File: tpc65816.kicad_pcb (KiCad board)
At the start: 2 copper layers, 100 x 100 mm, 51 parts, among them J1 Barrel_Jack, J2 PORTA, J3 PORTB, J4 SD_CARD, J5 PORTD, J6 PORTC, Q1 Q_PNP_BCE, Q2 Q_NPN_BCE, SW1 RESET, U1 74HC00, U10 WD65C22, U11 WD65C22, U2 74LS245, U3 L7805, U4 WD65C816S, U5 74LS573, U6 IS61C5128AS-25QLI, U7 28C256, U8 74F521, U9 74HC00

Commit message: Edit to main schematic and layout
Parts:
- SD CARD: renamed from J4
- moved BUSY 9.94 mm to (173.3, 109.2)
- moved R6 5.66 mm to (171.2, 99.6)
- moved C4 3.28 mm to (159.5, 82.0), turned to 270 degrees
- moved C5 3.02 mm to (139.4, 95.5), turned to 90 degrees
- moved R5 1.34 mm to (164.4, 102.1)
- moved Q2 0.44 mm to (163.3, 95.2)
- moved Q1 0.20 mm to (176.0, 100.7)
- renumbered D4 to BUSY, D3 to EMU, J2 to PORTA, J3 to PORTB, J6 to PORTC, J5 to PORTD, D2 to POWER, SW1 to RESET
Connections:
- U10 pad 39: GND -> (no net)
- U10 pad 40: GND -> (no net)
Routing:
- net +5V: track 669.7 -> 681.5 mm, vias 3 -> 2
- net Net-(D4-Pad1): track 2.36 -> 13.8 mm
- net Net-(D4-Pad2): track 3.66 -> 11.0 mm
- net Net-(Q2-Pad2): track 2.90 -> 7.28 mm
- net GND: vias 21 -> 17
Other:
- board text added: "PRELIMIARY"

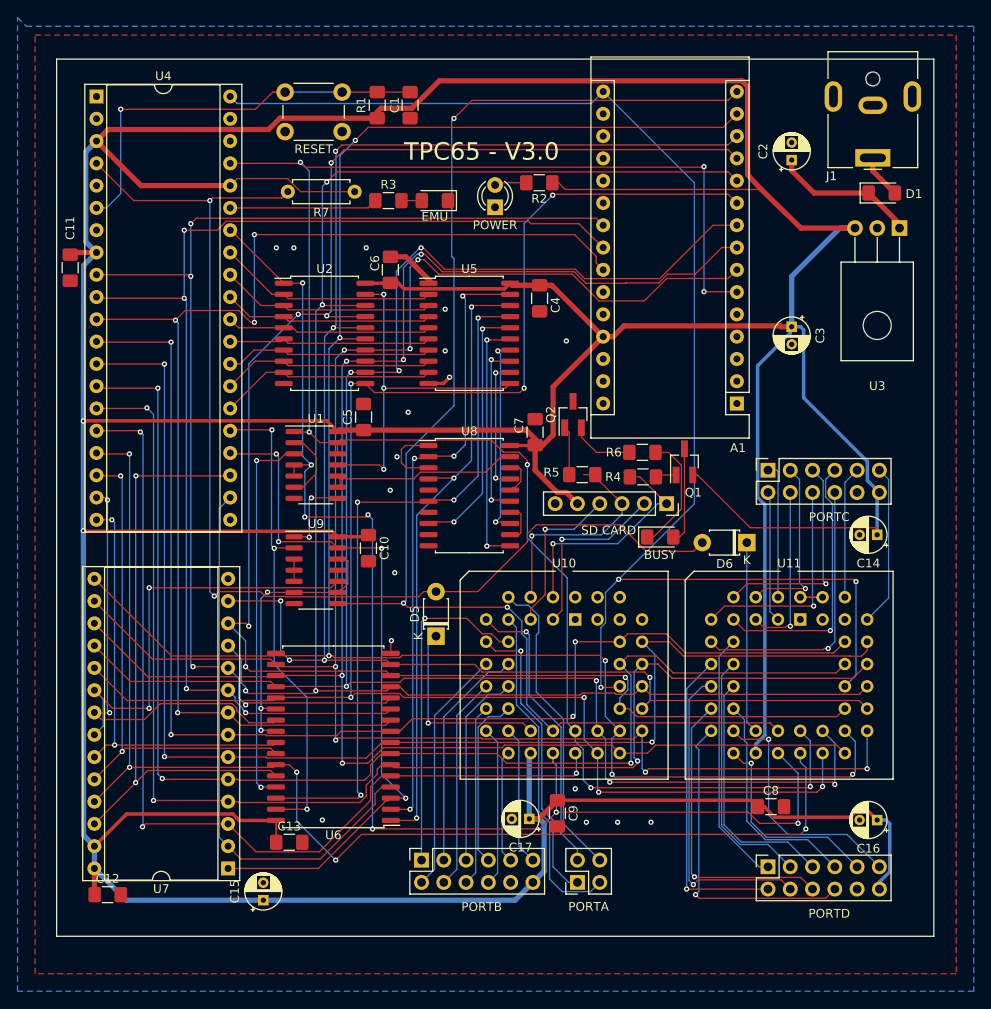
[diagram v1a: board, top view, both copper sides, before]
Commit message: Minor cleanup and repositioning - fabricated
Schematic verified. Added power switch. Repositioned PORT A. Cleanup of some traces. Added silkscreen markings. 

Board has been sent to fabrication as of this commit.
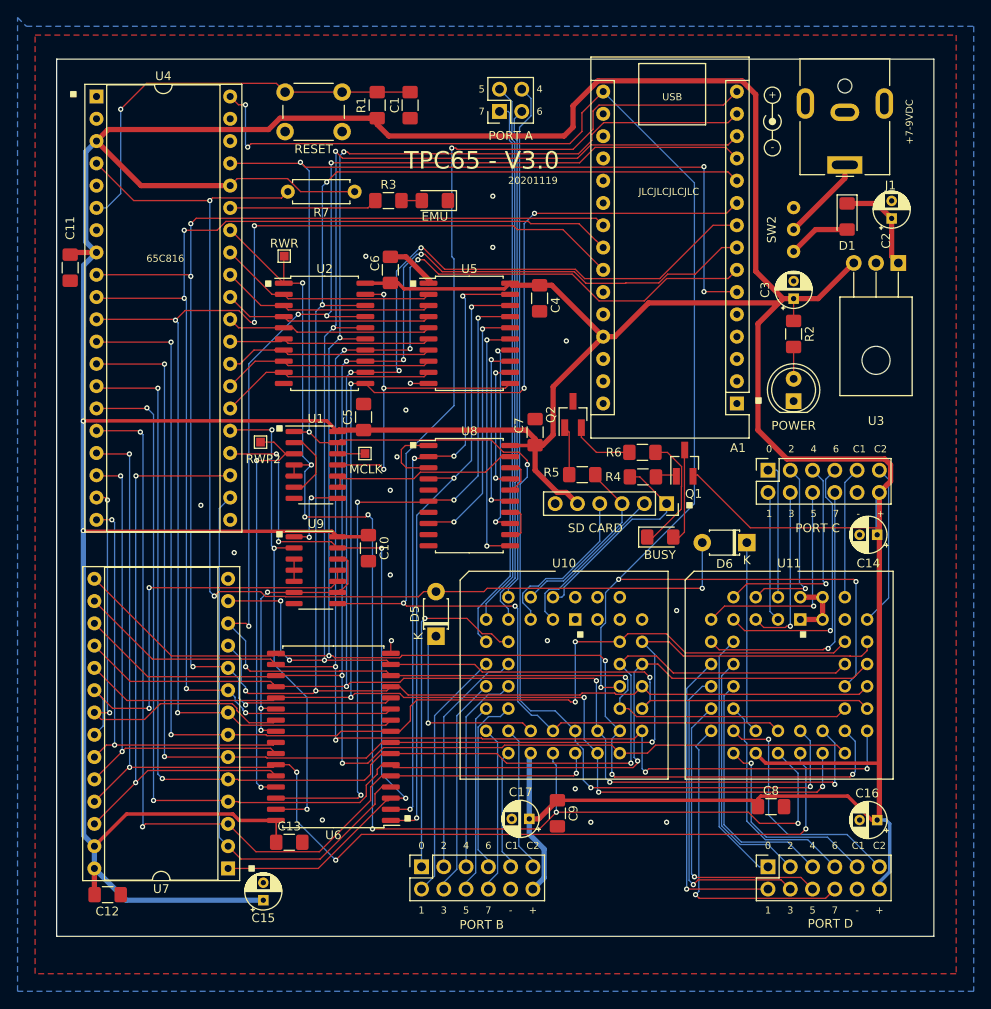
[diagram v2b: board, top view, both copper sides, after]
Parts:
- removed PORTA: PORTA, Connector_PinSocket_2.54mm:PinSocket_2x02_P2.54mm_Vertical
- removed the POWER at (154.4, 71.6)
- added MCLK: MCLK, TestPoint:TestPoint_Pad_1.0x1.0mm, F.Cu at (139.6, 99.7)
- added PORT A: PORTA, Connector_PinSocket_2.54mm:PinSocket_2x02_P2.54mm_Vertical, F.Cu at (154.9, 60.7)
- added POWER: POWERLED, LED_THT:LED_D5.0mm, F.Cu at (188.5, 93.7)
- added REF**: Symbol_Barrel_Polarity, Symbol:Symbol_Barrel_Polarity, F.Cu at (186.0, 61.9)
- added RWP2: RW_PH2, TestPoint:TestPoint_Pad_1.0x1.0mm, F.Cu at (127.7, 98.4)
- added RWR: RW_RAW, TestPoint:TestPoint_Pad_1.0x1.0mm, F.Cu at (130.4, 77.2)
- added SW2: SW_SPDT, slide_switch:spdt_slide_switch, F.Cu at (188.5, 74.2)
- PORT B: renamed from PORTB
- PORT C: renamed from PORTC
- PORT D: renamed from PORTD
- moved R2 33.7 mm to (188.5, 86.1), turned to 270 degrees
- moved C2 13.2 mm to (199.6, 72.9)
- moved D1 4.77 mm to (194.6, 72.7), turned to 270 degrees
- moved U3 3.98 mm to (200.4, 78.0)
- moved J1 3.29 mm to (194.3, 66.8)
- moved C3 3.22 mm to (188.5, 82.0), turned to 90 degrees
- moved PORT B 0.76 mm to (146.1, 146.8)
- moved Q1 0.15 mm to (176.1, 100.8)
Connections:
- J1 pad 1: Net-(D1-Pad2) -> Net-(J1-Pad1)
- J1 pad MP: (no net) -> GND
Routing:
- net +5V: track 681.5 -> 642.4 mm
- net /Sheet60C81ED6/PA7: track 34.0 -> 63.6 mm, vias 1 -> 0
- net /Sheet60C81ED6/PA5: track 33.6 -> 62.5 mm, vias 1 -> 0
- net /Sheet60C81ED6/PA4: track 35.3 -> 59.4 mm
- net /Sheet60C81ED6/PA6: track 38.3 -> 59.6 mm
- net Net-(J1-Pad1): track 0.00 -> 9.79 mm
- net ~RESET: track 161.9 -> 169.9 mm, vias 3 -> 5
- net PH2: track 205.2 -> 210.6 mm
- net Net-(C2-Pad1): track 16.5 -> 11.2 mm
- net /Sheet60C81ED6/PA2: track 25.3 -> 20.8 mm, vias 1 -> 0
- net GND: track 29.9 -> 34.3 mm, vias 17 -> 18
- net RW_PH2: track 43.8 -> 47.2 mm
- net RW_RAW: track 151.4 -> 154.5 mm
- net /Sheet60C81ED6/PA0: track 26.4 -> 23.9 mm, vias 1 -> 0
- net Net-(D1-Pad2): track 5.04 -> 7.13 mm
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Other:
- board text added: "+"
- board text added: "+7-9VDC"
- board text added: "-"
- board text added: "0"
- board text added: "1"
- board text added: "2"
- board text added: "20201119"
- board text added: "3"
- board text added: "4"
- board text added: "5"
- board text added: "6"
- board text added: "65C816"
- board text added: "7"
- board text added: "C1"
- board text added: "C2"
- board text added: "JLCJLCJLCJLC"
- board text added: "USB"
- board text removed: "PRELIMIARY"

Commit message: Fixed floating rdy pin
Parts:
-  : renamed from SW2
- renumbered MCLK to TP1, RWR to TP2, RWP2 to TP3
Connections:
-   pad 3: (no net) -> Net-(SW2-Pad3)
- A1 pad 1: (no net) -> Net-(A1-Pad1)
- A1 pad 17: (no net) -> Net-(A1-Pad17)
- A1 pad 18: (no net) -> Net-(A1-Pad18)
- A1 pad 19: (no net) -> Net-(A1-Pad19)
- A1 pad 2: (no net) -> Net-(A1-Pad2)
- A1 pad 20: (no net) -> Net-(A1-Pad20)
- A1 pad 21: (no net) -> Net-(A1-Pad21)
- A1 pad 25: (no net) -> Net-(A1-Pad25)
- A1 pad 26: (no net) -> Net-(A1-Pad26)
- A1 pad 28: (no net) -> Net-(A1-Pad28)
- A1 pad 3: (no net) -> Net-(A1-Pad3)
- A1 pad 30: (no net) -> Net-(A1-Pad30)
- A1 pad 5: (no net) -> Net-(A1-Pad5)
- J1 pad MP: GND -> (no net)
- U10 pad 39: (no net) -> Net-(U10-Pad39)
- U10 pad 40: (no net) -> Net-(U10-Pad40)
- U10 pad 41: GND -> (no net)
- U10 pad 42: GND -> (no net)
- U10 pad 43: GND -> (no net)
- U10 pad 44: GND -> (no net)
- U11 pad 41: GND -> (no net)
- U11 pad 42: GND -> (no net)
- U11 pad 43: GND -> (no net)
- U11 pad 44: GND -> (no net)
- U4 pad 1: (no net) -> Net-(U4-Pad1)
- U4 pad 2: (no net) -> +5V
- U4 pad 38: (no net) -> Net-(U4-Pad38)
- U4 pad 39: (no net) -> Net-(U4-Pad39)
- U4 pad 5: (no net) -> Net-(U4-Pad5)
- U4 pad 7: (no net) -> Net-(U4-Pad7)
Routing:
- net +5V: track 642.4 -> 644.9 mm
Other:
- board text added: "OFF ON"

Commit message: Fill update
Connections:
- U10 pad 41: (no net) -> GND
- U10 pad 42: (no net) -> GND
- U10 pad 43: (no net) -> GND
- U10 pad 44: (no net) -> GND
- U11 pad 41: (no net) -> GND
- U11 pad 42: (no net) -> GND
- U11 pad 43: (no net) -> GND
- U11 pad 44: (no net) -> GND
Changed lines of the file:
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@@
   )
   (setup
-    (last_trace_width 0.2)
+    (last_trace_width 0.127)
     (user_trace_width 0.15)
     (user_trace_width 0.2)
@@
     (mod_text_size 0.8128 0.8128)
     (mod_text_width 0.1524)
-    (pad_size 2 3.5)
-    (pad_drill 1)
+    (pad_size 1.4224 1.4224)
+    (pad_drill 0.8)
     (pad_to_mask_clearance 0)
     (solder_mask_min_width 0.12)
@@
     (pad 8 thru_hole circle (at -7.62 0) (size 1.4224 1.4224) (drill 0.8) (layers *.Cu *.Mask)
       (net 65 /Sheet60C81ED6/PA6))
-    (pad 42 thru_hole circle (at 2.54 -2.54) (size 1.4224 1.4224) (drill 0.8) (layers *.Cu *.Mask))
-    (pad 44 thru_hole circle (at 0 -2.54) (size 1.4224 1.4224) (drill 0.8) (layers *.Cu *.Mask))
+    (pad 42 thru_hole circle (at 2.54 -2.54) (size 1.4224 1.4224) (drill 0.8) (layers *.Cu *.Mask)
+      (net 2 GND))
+    (pad 44 thru_hole circle (at 0 -2.54) (size 1.4224 1.4224) (drill 0.8) (layers *.Cu *.Mask)
+      (net 2 GND))
     (pad 6 thru_hole circle (at -7.62 -2.54) (size 1.4224 1.4224) (drill 0.8) (layers *.Cu *.Mask)
       (net 67 /Sheet60C81ED6/PA4))
@@
     (pad 2 thru_hole circle (at -2.54 -2.54) (size 1.4224 1.4224) (drill 0.8) (layers *.Cu *.Mask)
       (net 78 /Sheet60C81ED6/PA0))
-    (pad 41 thru_hole circle (at 5.08 0) (size 1.4224 1.4224) (drill 0.8) (layers *.Cu *.Mask))
-    (pad 43 thru_hole circle (at 2.54 0) (size 1.4224 1.4224) (drill 0.8) (layers *.Cu *.Mask))
+    (pad 41 thru_hole circle (at 5.08 0) (size 1.4224 1.4224) (drill 0.8) (layers *.Cu *.Mask)
+      (net 2 GND))
+    (pad 43 thru_hole circle (at 2.54 0) (size 1.4224 1.4224) (drill 0.8) (layers *.Cu *.Mask)
+      (net 2 GND))
     (pad 5 thru_hole circle (at -5.08 0) (size 1.4224 1.4224) (drill 0.8) (layers *.Cu *.Mask)
       (net 81 /Sheet60C81ED6/PA3))
@@
     (pad 5 thru_hole circle (at -5.08 0) (size 1.4224 1.4224) (drill 0.8) (layers *.Cu *.Mask)
       (net 95 /Sheet60C81ED6/PC3))
-    (pad 43 thru_hole circle (at 2.54 0) (size 1.4224 1.4224) (drill 0.8) (layers *.Cu *.Mask))
-    (pad 41 thru_hole circle (at 5.08 0) (size 1.4224 1.4224) (drill 0.8) (layers *.Cu *.Mask))
+    (pad 43 thru_hole circle (at 2.54 0) (size 1.4224 1.4224) (drill 0.8) (layers *.Cu *.Mask)
+      (net 2 GND))
+    (pad 41 thru_hole circle (at 5.08 0) (size 1.4224 1.4224) (drill 0.8) (layers *.Cu *.Mask)
+      (net 2 GND))
     (pad 2 thru_hole circle (at -2.54 -2.54) (size 1.4224 1.4224) (drill 0.8) (layers *.Cu *.Mask)
       (net 92 /Sheet60C81ED6/PC0))
@@
     (pad 6 thru_hole circle (at -7.62 -2.54) (size 1.4224 1.4224) (drill 0.8) (layers *.Cu *.Mask)
       (net 96 /Sheet60C81ED6/PC4))
-    (pad 44 thru_hole circle (at 0 -2.54) (size 1.4224 1.4224) (drill 0.8) (layers *.Cu *.Mask))
-    (pad 42 thru_hole circle (at 2.54 -2.54) (size 1.4224 1.4224) (drill 0.8) (layers *.Cu *.Mask))
+    (pad 44 thru_hole circle (at 0 -2.54) (size 1.4224 1.4224) (drill 0.8) (layers *.Cu *.Mask)
+      (net 2 GND))
+    (pad 42 thru_hole circle (at 2.54 -2.54) (size 1.4224 1.4224) (drill 0.8) (layers *.Cu *.Mask)
+      (net 2 GND))
     (pad 8 thru_hole circle (at -7.62 0) (size 1.4224 1.4224) (drill 0.8) (layers *.Cu *.Mask)
       (net 98 /Sheet60C81ED6/PC6))

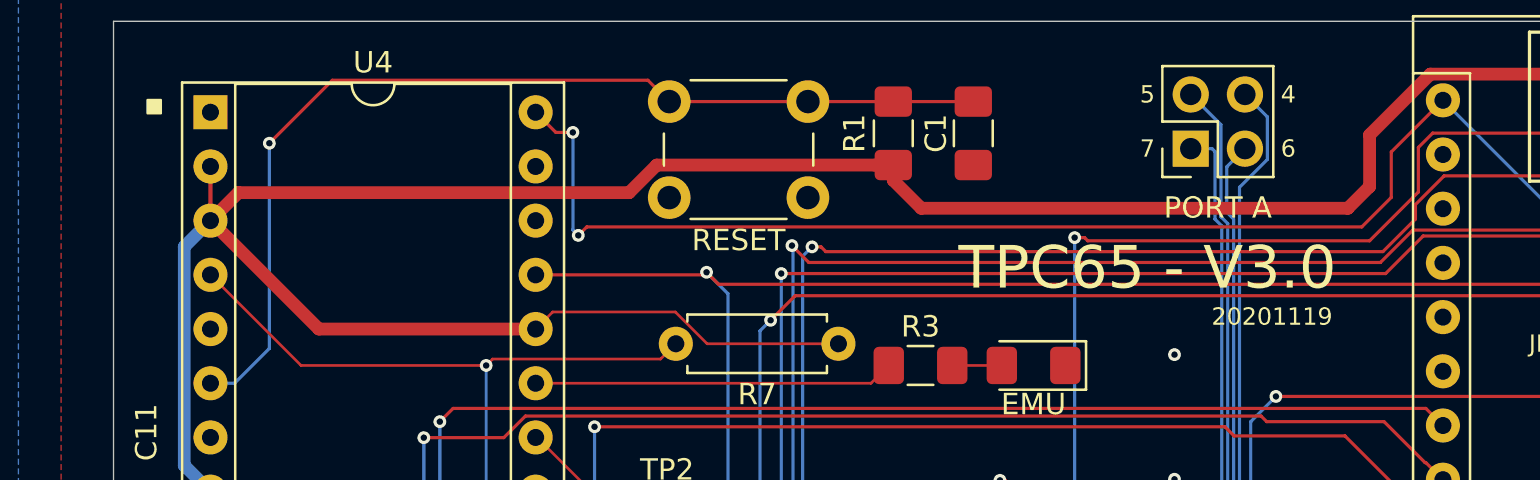
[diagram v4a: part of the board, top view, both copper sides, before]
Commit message: Fix to RDY pin
RDY needs to be pulled up with a resistor and not linked to VDD directly. Unlike the 65c02, RDY on the 65c816 is bidirectional and can, under some circumstances, attempt to pull itself down. If it's directly connected to VDD, it will attempt to sink VDD and short out. WDC seems to recommend using 3.3K resistors as pullups. I'm not sure how other values would perform. BE is now pulled up with a resistor too, which is recommended by WDC for reasons I'm not sure about.
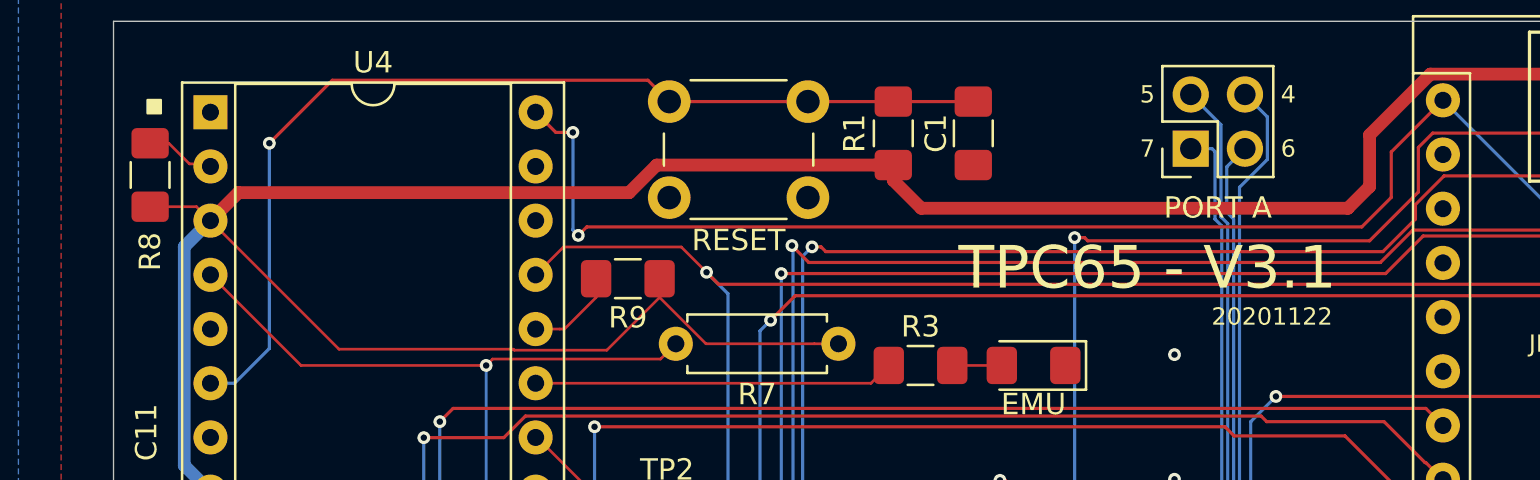
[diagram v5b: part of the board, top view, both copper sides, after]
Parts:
- added R8: 3.3k, Resistor_SMD:R_1206_3216Metric_Pad1.42x1.75mm_HandSolder, F.Cu at (106.2, 61.9)
- added R9: 3.3k, Resistor_SMD:R_1206_3216Metric_Pad1.42x1.75mm_HandSolder, F.Cu at (128.6, 66.8)
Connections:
- U4 pad 2: +5V -> Net-(R8-Pad2)
- U4 pad 36: +5V -> Net-(R9-Pad2)
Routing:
- net Net-(R9-Pad2): track 0.00 -> 4.32 mm
- net Net-(R8-Pad2): track 0.00 -> 3.06 mm
- net +5V: track 644.9 -> 647.7 mm
- net PH2: track 210.6 -> 211.8 mm
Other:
- board text added: "20201122"
- board text added: "TPC65 - V3.1"
- board text removed: "20201119"
- board text removed: "TPC65 - V3.0"

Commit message: Track cleanup
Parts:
- moved C15 2.74 mm to (129.4, 148.3), turned to 0 degrees
- moved Q2 2.57 mm to (163.4, 97.8)
- moved BUSY 1.36 mm to (172.0, 109.6)
- renumbered TP3 to RWP, TP2 to RWR
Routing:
- net ~RESET: track 169.9 -> 146.8 mm, vias 5 -> 2
- net +5V: track 647.7 -> 630.2 mm, vias 2 -> 3
- net A12: track 63.9 -> 80.0 mm
- net Net-(J3-Pad11): track 15.9 -> 28.5 mm
- net A8: track 140.5 -> 128.9 mm
- net /Sheet60C81ED6/PA0: track 23.9 -> 34.0 mm
- net Net-(J3-Pad9): track 12.9 -> 22.2 mm
- net A22: track 20.4 -> 29.6 mm
- net /Sheet60C81ED6/PD7: track 36.2 -> 27.2 mm
- net /Sheet60C81ED6/PA1: track 18.9 -> 27.4 mm
- net A21: track 23.0 -> 30.7 mm
- net A23: track 15.4 -> 23.0 mm
- net DB1: track 193.3 -> 200.7 mm, vias 6 -> 5
- net /Sheet60C81ED6/PC1: track 15.0 -> 22.2 mm
- net /Sheet60C81ED6/PD3: track 36.1 -> 29.6 mm
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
